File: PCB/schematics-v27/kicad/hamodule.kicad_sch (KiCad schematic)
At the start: 206 parts, among them J1 GND|5V, J10 Tx|Rx, J11 Sda|Scl, J12 3|9, J13 13|12, J14 3.3v|GND|7|15, J15 2604-1104, J16 2604-1104, J17 TestPoint, J19 TestPoint, J2 2604-1102, J3 USB_C_Receptacle_USB2.0, J4 GND|3.3V, J5 Jumper 3.3v, J6 2604-1104, J7 2604-1104, J8 5v|GND|Do, J9 Screen, K1 AQG22205, K2 AQG22205, K3 AQG22205, K4 AQG22205, K5 AQG22205, K6 AQG22205, K7 AQG22205, K8 AQG22205, SW1 USB | PS, SW2 Reset, SW3 Boot, U1 LD1117AV33, U10 SN74LV1T34DBV, U11 ULN2803A, U12 TCAL6416, U14 74AHC1G04, U2 USBLC6-2SC6, U3 ESP32-S3-WROOM-2, U4 LDA210, U5 LDA210, U6 LDA210, U7 LDA210, U8 SHT4x, U9 SN74LVCH8T245

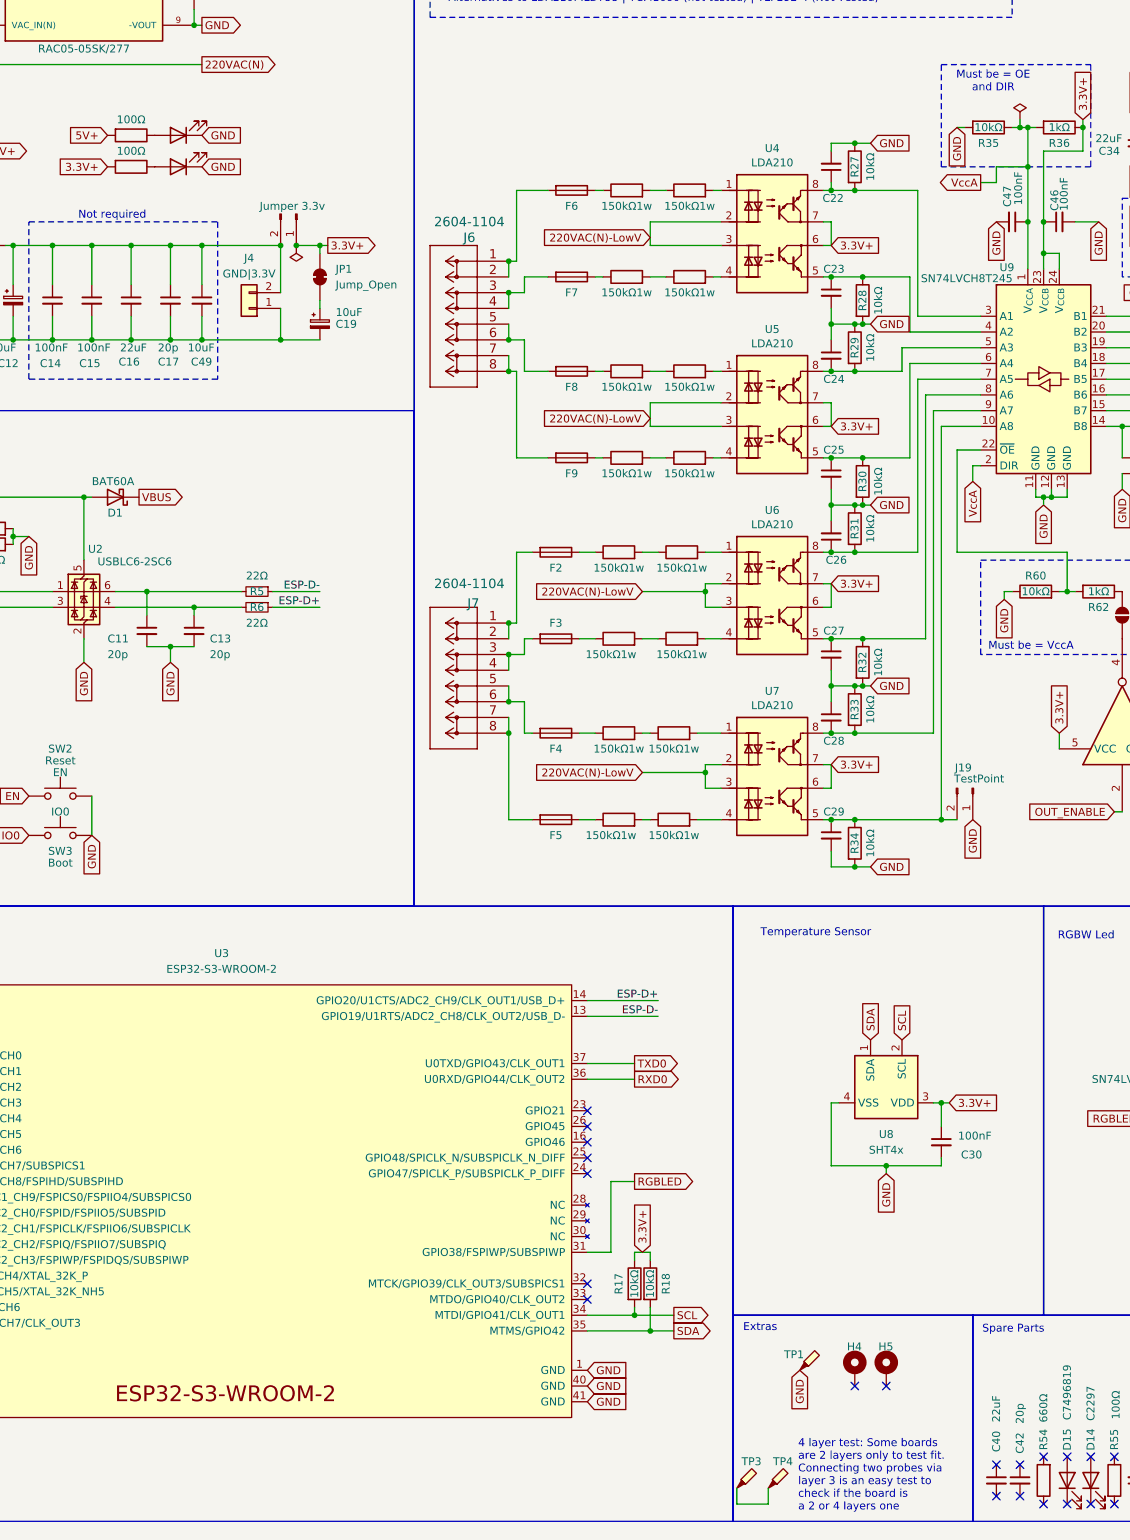
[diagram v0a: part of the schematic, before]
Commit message: thicker traces for mains going to relays, in preparation for larger fuses. Moved 4 layer testers. Added vias for 3.3V traces in both layers
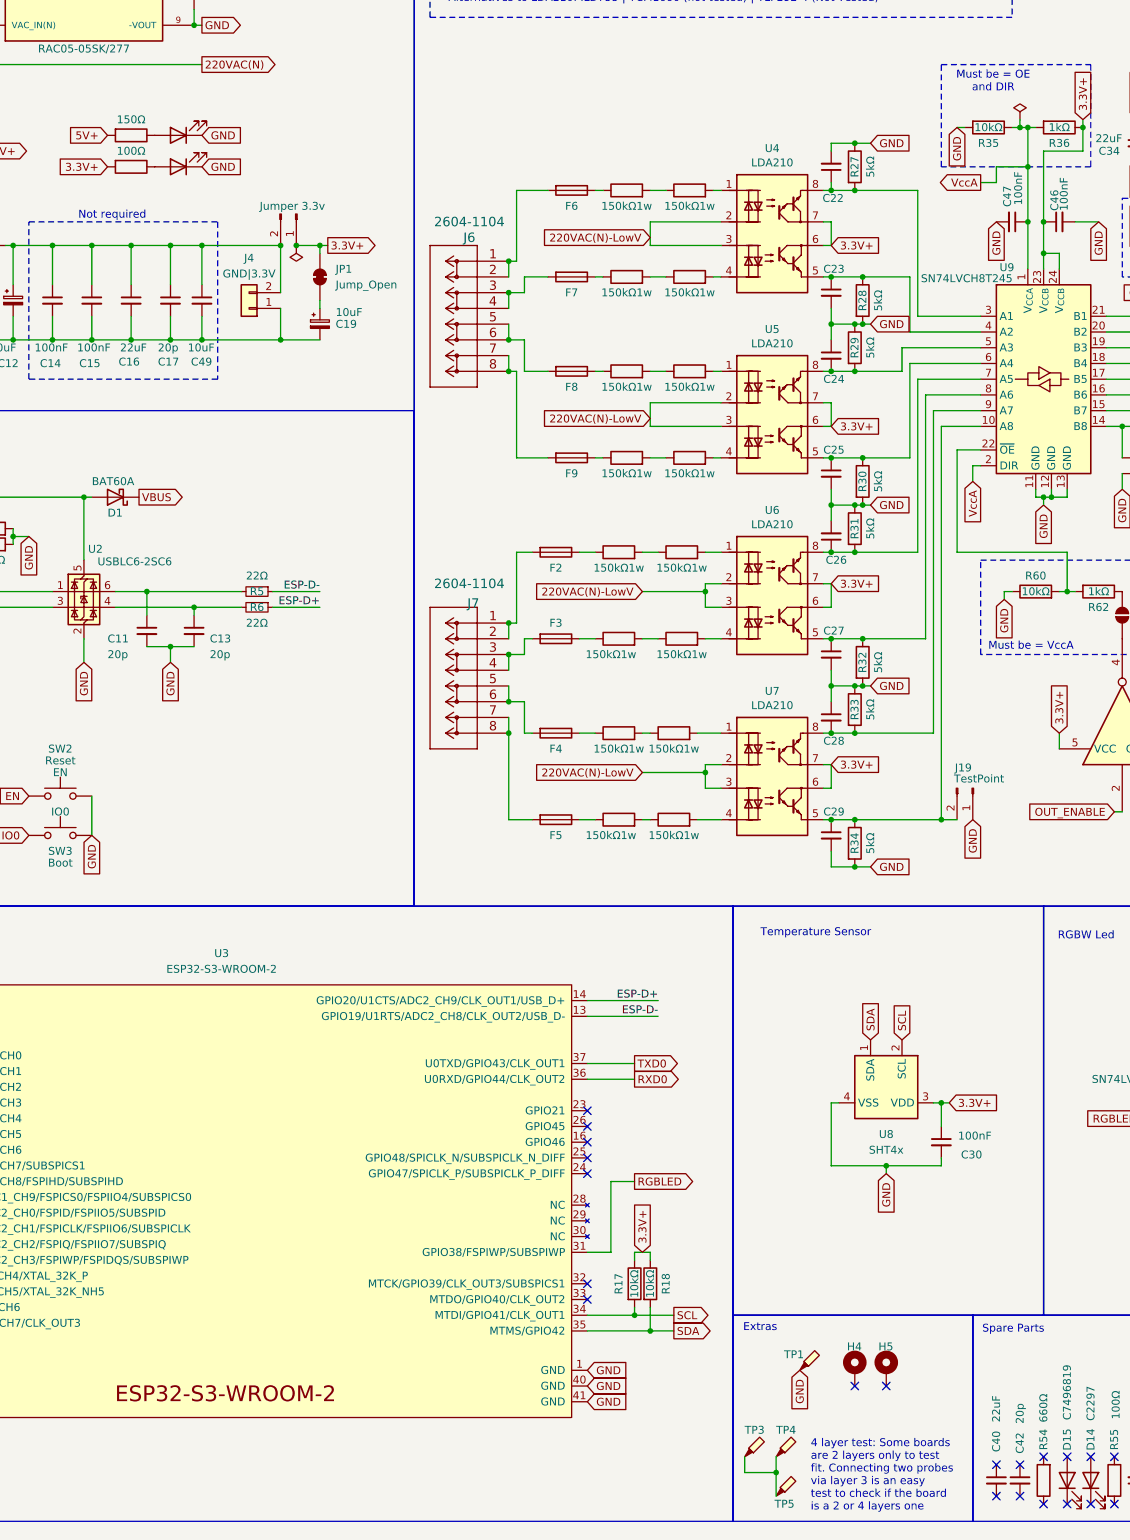
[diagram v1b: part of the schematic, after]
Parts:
- added TP5: 4 layer test, TestPoint:TestPoint_THTPad_1.0x1.0mm_Drill0.5mm, symbol Connector:TestPoint_Probe
- R27, R28, R29, R30, R31, R32, R33, R34: value 10kΩ -> 5kΩ; JLCPCB C25804 -> (none); LCSC C25804 -> (none)
- R7: value 100Ω -> 150Ω; JLCPCB C17408 -> (none); LCSC C17408 -> (none)
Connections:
- net at TP3.1, TP4.1: now also TP5.1
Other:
- moved on the sheet: TP3, TP4

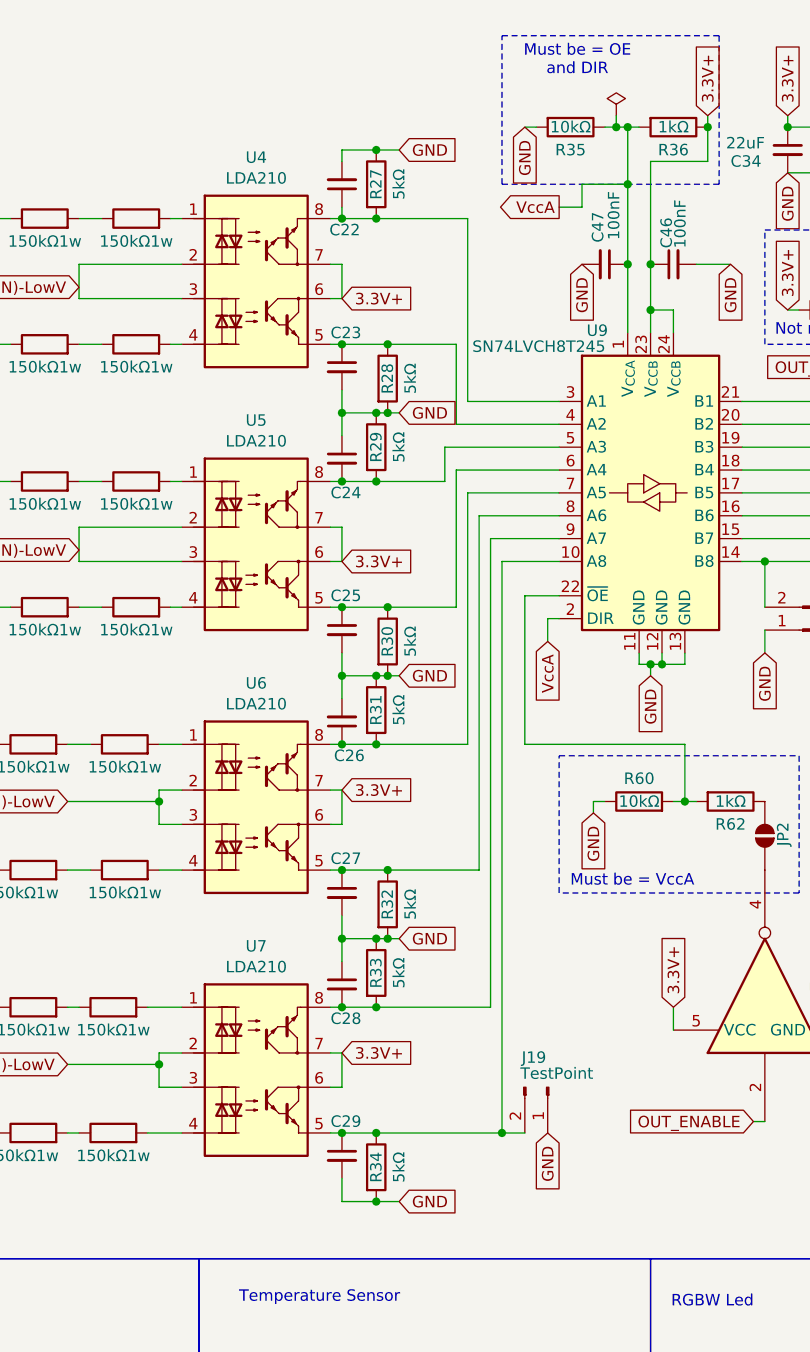
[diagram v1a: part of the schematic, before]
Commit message: [v27] uses now 1k resistor as pull down for TCAL read port. Updated schematic and PCB with V27
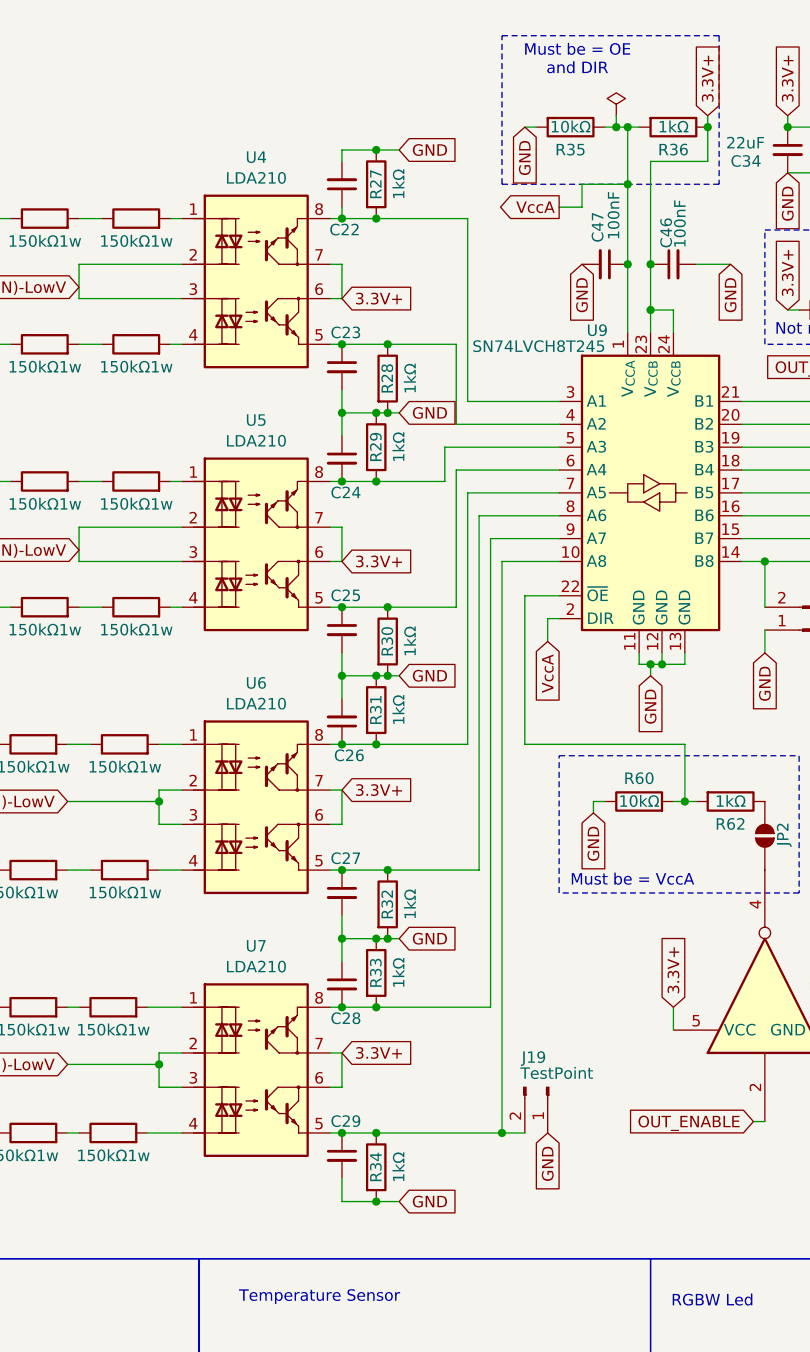
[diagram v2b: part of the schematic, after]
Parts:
- R27, R28, R29, R30, R31, R32, R33, R34: value 5kΩ -> 1kΩ; JLCPCB (none) -> C21190; LCSC (none) -> C21190
- R7: JLCPCB (none) -> C17437; LCSC (none) -> C17437
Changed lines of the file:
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@@
 	(title_block
 		(title "Home Assistant module for lights control")
-		(date "2025-08-19")
-		(rev "20250819.26.1.2L")
+		(date "2025-11-26")
+		(rev "20251126.27")
 	)
 	(rectangle
@@
 			)
 		)
-		(property "JLCPCB" ""
+		(property "JLCPCB" "C17437"
 			(at 88.9 59.69 0)
 			(effects
@@
 			)
 		)
-		(property "LCSC" ""
+		(property "LCSC" "C17437"
 			(at 88.9 59.69 0)
 			(effects
@@
 			)
 		)
-		(property "Value" "5kΩ"
+		(property "Value" "1kΩ"
 			(at 209.55 144.78 90)
 			(effects
@@
 			)
 		)
-		(property "JLCPCB" ""
+		(property "JLCPCB" "C21190"
 			(at 207.01 144.78 0)
 			(effects
@@
 			)
 		)
-		(property "LCSC" ""
+		(property "LCSC" "C21190"
 			(at 207.01 144.78 0)
 			(effects
@@
 			)
 		)
-		(property "Value" "5kΩ"
+		(property "Value" "1kΩ"
 			(at 209.55 115.57 90)
 			(effects
@@
 			)
 		)
-		(property "JLCPCB" ""
+		(property "JLCPCB" "C21190"
 			(at 207.01 115.57 0)
 			(effects
@@
 			)
 		)
-		(property "LCSC" ""
+		(property "LCSC" "C21190"
 			(at 207.01 115.57 0)
 			(effects
@@
 			)
 		)
-		(property "Value" "5kΩ"
+		(property "Value" "1kΩ"
 			(at 208.28 93.98 90)
 			(effects
@@
 			)
 		)
-		(property "JLCPCB" ""
+		(property "JLCPCB" "C21190"
 			(at 205.74 93.98 0)
 			(effects
@@
 			)
 		)
-		(property "LCSC" ""
+		(property "LCSC" "C21190"
 			(at 205.74 93.98 0)
 			(effects
@@
 			)
 		)
-		(property "Value" "5kΩ"
+		(property "Value" "1kΩ"
 			(at 208.28 123.19 90)
 			(effects
@@
 			)
 		)
-		(property "JLCPCB" ""
+		(property "JLCPCB" "C21190"
 			(at 205.74 123.19 0)
 			(effects
@@
 			)
 		)
-		(property "LCSC" ""
+		(property "LCSC" "C21190"
 			(at 205.74 123.19 0)
 			(effects
@@
 			)
 		)
-		(property "Value" "5kΩ"
+		(property "Value" "1kΩ"
 			(at 209.55 86.36 90)
 			(effects
@@
 			)
 		)
-		(property "JLCPCB" ""
+		(property "JLCPCB" "C21190"
 			(at 207.01 86.36 0)
 			(effects
@@
 			)
 		)
-		(property "LCSC" ""
+		(property "LCSC" "C21190"
 			(at 207.01 86.36 0)
 			(effects
@@
 			)
 		)
-		(property "Value" "5kΩ"
+		(property "Value" "1kΩ"
 			(at 208.28 64.77 90)
 			(effects
@@
 			)
 		)
-		(property "JLCPCB" ""
+		(property "JLCPCB" "C21190"
 			(at 205.74 64.77 0)
 			(effects
@@
 			)
 		)
-		(property "LCSC" ""
+		(property "LCSC" "C21190"
 			(at 205.74 64.77 0)
 			(effects
@@
 			)
 		)
-		(property "Value" "5kΩ"
+		(property "Value" "1kΩ"
 			(at 208.28 173.99 90)
 			(effects
@@
 			)
 		)
-		(property "JLCPCB" ""
+		(property "JLCPCB" "C21190"
 			(at 205.74 173.99 0)
 			(effects
@@
 			)
 		)
-		(property "LCSC" ""
+		(property "LCSC" "C21190"
 			(at 205.74 173.99 0)
 			(effects
@@
 			)
 		)
-		(property "Value" "5kΩ"
+		(property "Value" "1kΩ"
 			(at 208.28 152.4 90)
 			(effects
@@
 			)
 		)
-		(property "JLCPCB" ""
+		(property "JLCPCB" "C21190"
 			(at 205.74 152.4 0)
 			(effects
@@
 			)
 		)
-		(property "LCSC" ""
+		(property "LCSC" "C21190"
 			(at 205.74 152.4 0)
 			(effects

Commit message: [v27] updated to the latest kicad version v10
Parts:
- JP2: value ~ -> (none)
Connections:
- net at R2.1: now also J3.SH (SHIELD); no longer J3.S1 (SHIELD)
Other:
- moved on the sheet: JP2, U14

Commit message: [v27] Replaced small caps by 22uF. Reshuffled LED for 3.3V and 5V for more separation. Separate more 3.3v, 5v and jumper connection
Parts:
- C10, C14, C15, C20, C5: value 100nF -> 22uF; JLCPCB C49678 -> C45783
- C9: value 20p -> 22uF; footprint Capacitor_SMD:C_0603_1608Metric_Pad1.08x0.95mm_HandSolder -> Capacitor_SMD:C_0805_2012Metric_Pad1.18x1.45mm_HandSolder; LCSC C1648 -> C45783
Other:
- moved on the sheet: C10, C12, C14, C15, C16, C17, C20, C21, C48, C49, C9, J4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

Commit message: updating the version. updating part numbers for jlcpcb
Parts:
- C10, C14, C15, C20, C5: LCSC C49678 -> C45783
- C34: JLCPCB C59461 -> C45783; LCSC C59461 -> C45783
- C9: JLCPCB C1648 -> C45783
- J1, J4: JLCPCB C492401 -> C158012; LCSC C492401 -> C158012
- J14: value 3.3v|GND|7|15 -> j14; JLCPCB (none) -> C49257; LCSC (none) -> C49257
- J15, J16, J6, J7: JLCPCB (none) -> C3309598; LCSC (none) -> C3309598
- J9: JLCPCB (none) -> C32713270; LCSC (none) -> C32713270
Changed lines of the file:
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@@
 	(title_block
 		(title "Home Assistant module for lights control")
-		(date "2025-11-26")
-		(rev "20251126.27")
+		(date "2026-06-27")
+		(rev "20260627.27")
 	)
 	(rectangle
@@
 			)
 		)
-		(property "JLCPCB" "C492401"
+		(property "JLCPCB" "C158012"
 			(at 17.78 88.9 0)
 			(hide yes)
@@
 			)
 		)
-		(property "LCSC" "C492401"
+		(property "LCSC" "C158012"
 			(at 17.78 88.9 0)
 			(hide yes)
@@
 			)
 		)
-		(property "JLCPCB" "C492401"
+		(property "JLCPCB" "C158012"
 			(at 105.41 87.63 0)
 			(hide yes)
@@
 			)
 		)
-		(property "LCSC" "C492401"
+		(property "LCSC" "C158012"
 			(at 105.41 87.63 0)
 			(hide yes)
@@
 			)
 		)
+		(property "JLCPCB" "C3309598"
+			(at 139.7 146.05 0)
+			(hide yes)
+			(show_name no)
+			(do_not_autoplace no)
+			(effects
+				(font
+					(size 1.27 1.27)
+				)
+			)
+		)
+		(property "LCSC" "C3309598"
+			(at 139.7 146.05 0)
+			(hide yes)
+			(show_name no)
+			(do_not_autoplace no)
+			(effects
+				(font
+					(size 1.27 1.27)
+				)
+			)
+		)
 		(pin "1"
 		)
@@
 			)
 		)
+		(property "JLCPCB" "C3309598"
+			(at 403.86 91.44 0)
+			(hide yes)
+			(show_name no)
+			(do_not_autoplace no)
+			(effects
+				(font
+					(size 1.27 1.27)
+				)
+			)
+		)
+		(property "LCSC" "C3309598"
+			(at 403.86 91.44 0)
+			(hide yes)
+			(show_name no)
+			(do_not_autoplace no)
+			(effects
+				(font
+					(size 1.27 1.27)
+				)
+			)
+		)
 		(pin "1"
 		)
@@
 			)
 		)
-		(property "LCSC" "C49678"
+		(property "LCSC" "C45783"
 			(at 73.66 86.36 0)
 			(hide yes)
@@
 			)
 		)
+		(property "JLCPCB" "C3309598"
+			(at 403.86 146.05 0)
+			(hide yes)
+			(show_name no)
+			(do_not_autoplace no)
+			(effects
+				(font
+					(size 1.27 1.27)
+				)
+			)
+		)
+		(property "LCSC" "C3309598"
+			(at 403.86 146.05 0)
+			(hide yes)
+			(show_name no)
+			(do_not_autoplace no)
+			(effects
+				(font
+					(size 1.27 1.27)
+				)
+			)
+		)
 		(pin "1"
 		)
@@
 			)
 		)
-		(property "Value" "3.3v|GND|7|15"
+		(property "Value" "j14"
 			(at 391.16 228.6 90)
 			(show_name no)
@@
 			)
 		)
+		(property "JLCPCB" "C49257"
+			(at 389.89 223.52 90)
+			(hide yes)
+			(show_name no)
+			(do_not_autoplace no)
+			(effects
+				(font
+					(size 1.27 1.27)
+				)
+			)
+		)
+		(property "LCSC" "C49257"
+			(at 389.89 223.52 90)
+			(hide yes)
+			(show_name no)
+			(do_not_autoplace no)
+			(effects
+				(font
+					(size 1.27 1.27)
+				)
+			)
+		)
 		(pin "2"
 		)
@@
 			)
 		)
-		(property "LCSC" "C49678"
+		(property "LCSC" "C45783"
 			(at 48.26 86.36 0)
 			(hide yes)
@@
 			)
 		)
-		(property "LCSC" "C49678"
+		(property "LCSC" "C45783"
 			(at 367.03 35.56 0)
 			(hide yes)
@@
 			)
 		)
+		(property "JLCPCB" "C3309598"
+			(at 139.7 87.63 0)
+			(hide yes)
+			(show_name no)
+			(do_not_autoplace no)
+			(effects
+				(font
+					(size 1.27 1.27)
+				)
+			)
+		)
+		(property "LCSC" "C3309598"
+			(at 139.7 87.63 0)
+			(hide yes)
+			(show_name no)
+			(do_not_autoplace no)
+			(effects
+				(font
+					(size 1.27 1.27)
+				)
+			)
+		)
 		(pin "1"
 		)
@@
 			)
 		)
-		(property "JLCPCB" "C1648"
+		(property "JLCPCB" "C45783"
 			(at 377.19 35.56 0)
 			(hide yes)
@@
 			)
 		)
+		(property "JLCPCB" "C32713270"
+			(at 309.88 218.44 0)
+			(hide yes)
+			(show_name no)
+			(do_not_autoplace no)
+			(effects
+				(font
+					(size 1.27 1.27)
+				)
+			)
+		)
+		(property "LCSC" "C32713270"
+			(at 309.88 218.44 0)
+			(hide yes)
+			(show_name no)
+			(do_not_autoplace no)
+			(effects
+				(font
+					(size 1.27 1.27)
+				)
+			)
+		)
 		(pin "1"
 		)
@@
 			)
 		)
-		(property "LCSC" "C49678"
+		(property "LCSC" "C45783"
 			(at 29.21 86.36 0)
 			(hide yes)
@@
 			)
 		)
-		(property "LCSC" "C49678"
+		(property "LCSC" "C45783"
 			(at 78.74 86.36 0)
 			(hide yes)
@@
 			)
 		)
-		(property "JLCPCB" "C59461"
+		(property "JLCPCB" "C45783"
 			(at 251.46 60.96 0)
 			(hide yes)
@@
 			)
 		)
-		(property "LCSC" "C59461"
+		(property "LCSC" "C45783"
 			(at 251.46 60.96 0)
 			(hide yes)
